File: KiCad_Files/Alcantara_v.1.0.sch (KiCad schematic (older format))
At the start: 21 parts, among them IC3 TLV803EA30DCKR, J5 PJS008U-3000-0, J8 53261-0527, Q1 MMSS8050-H-TP, Q2 MMSS8050-H-TP

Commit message: Add shapes 3D folder
Now all 3D models for the components are stored in a single folder, thanks to the Archive Plugin from https://github.com/MitjaNemec/Kicad_action_plugins.git
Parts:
- C1, C2, C3, C4, C5: symbol Device:C_Small -> archive:Device_C_Small
- IC3: symbol SamacSys_Parts:TLV803EA30DCKR -> archive:SamacSys_Parts_TLV803EA30DCKR
- J5: symbol SamacSys_Parts:PJS008U-3000-0 -> archive:SamacSys_Parts_PJS008U-3000-0
- J8: symbol SamacSys_Parts:53261-0527 -> archive:SamacSys_Parts_53261-0527
- MOD1: symbol dk_RF-Transceiver-Modules:ESP32-WROOM-32 -> archive:dk_RF-Transceiver-Modules_ESP32-WROOM-32
- Q1, Q2: symbol dk_Transistors-Bipolar-BJT-Single:MMSS8050-H-TP -> archive:dk_Transistors-Bipolar-BJT-Single_MMSS8050-H-TP
- R1, R13, R2, R26, R3, R4, R5, R6: symbol Device:R_Small -> archive:Device_R_Small
- S4, S5: symbol SamacSys_Parts:EVP-AAM02W -> archive:SamacSys_Parts_EVP-AAM02W
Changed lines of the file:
@@
 $EndSheet
 $Comp
-L power:GND #PWR01
+L archive:power_GND #PWR01
 U 1 1 61138544
 P 2350 3750
@@
 	2400 3700 2500 3700
 $Comp
-L Device:C_Small C5
+L archive:Device_C_Small C5
 U 1 1 61143841
 P 7900 1575
@@
 $EndComp
 $Comp
-L power:GND #PWR06
+L archive:power_GND #PWR06
 U 1 1 61144448
 P 7900 1875
@@
 	7900 1475 7900 1275
 $Comp
-L power:+3V3 #PWR07
+L archive:power_+3V3 #PWR07
 U 1 1 61144E10
 P 7900 975
@@
 $EndComp
 $Comp
-L Device:R_Small R4
+L archive:Device_R_Small R4
 U 1 1 6114538C
 P 7900 1125
@@
 	9750 5650 9850 5650
 $Comp
-L dk_RF-Transceiver-Modules:ESP32-WROOM-32 MOD1
+L archive:dk_RF-Transceiver-Modules_ESP32-WROOM-32 MOD1
 U 1 1 60CDB9CF
 P 2200 1500
@@
 	3150 1000 3150 1050
 $Comp
-L power:GND #PWR04
+L archive:power_GND #PWR04
 U 1 1 6114294E
 P 3150 1250
@@
 $EndComp
 $Comp
-L Device:C_Small C2
+L archive:Device_C_Small C2
 U 1 1 61142948
 P 3150 1150
@@
 	2700 1000 2700 1050
 $Comp
-L power:GND #PWR02
+L archive:power_GND #PWR02
 U 1 1 611407CF
 P 2700 1250
@@
 $EndComp
 $Comp
-L Device:C_Small C1
+L archive:Device_C_Small C1
 U 1 1 611407C9
 P 2700 1150
@@
 $EndComp
 $Comp
-L power:+3V3 #PWR03
+L archive:power_+3V3 #PWR03
 U 1 1 61138053
 P 3150 950
@@
 	2400 1000 2700 1000
 $Comp
-L Device:C_Small C4
+L archive:Device_C_Small C4
 U 1 1 611FBCA3
 P 7550 1575
@@
 	9750 5000 9850 5000
 $Comp
-L dk_Transistors-Bipolar-BJT-Single:MMSS8050-H-TP Q1
+L archive:dk_Transistors-Bipolar-BJT-Single_MMSS8050-H-TP Q1
 U 1 1 61214E60
 P 5800 4875
@@
 $EndComp
 $Comp
-L dk_Transistors-Bipolar-BJT-Single:MMSS8050-H-TP Q2
+L archive:dk_Transistors-Bipolar-BJT-Single_MMSS8050-H-TP Q2
 U 1 1 61215ACB
 P 5800 5475
@@
 $EndComp
 $Comp
-L Device:R_Small R1
+L archive:Device_R_Small R1
 U 1 1 61216528
 P 5450 4875
@@
 $EndComp
 $Comp
-L Device:R_Small R2
+L archive:Device_R_Small R2
 U 1 1 61216A1C
 P 5450 5475
@@
 	7900 1275 8100 1275
 $Comp
-L power:GND #PWR05
+L archive:power_GND #PWR05
 U 1 1 612BFDFC
 P 5900 3650
@@
 $EndComp
 $Comp
-L Device:C_Small C3
+L archive:Device_C_Small C3
 U 1 1 612BFE20
 P 5900 3300
@@
 	3100 3000 3150 3000
 $Comp
-L power:+3V3 #PWR053
+L archive:power_+3V3 #PWR053
 U 1 1 614C013F
 P 7075 3425
@@
 $EndComp
 $Comp
-L power:+5V #PWR051
+L archive:power_+5V #PWR051
 U 1 1 614C4F85
 P 8375 3425
@@
 	7525 3525 7525 3375
 $Comp
-L power:GND #PWR052
+L archive:power_GND #PWR052
 U 1 1 614FBA5A
 P 7725 3675
@@
 	3650 2500 3650 2400
 $Comp
-L SamacSys_Parts:EVP-AAM02W S5
+L archive:SamacSys_Parts_EVP-AAM02W S5
 U 1 1 60E2AB97
 P 4450 3250
@@
 	5700 3350 5700 3550
 $Comp
-L SamacSys_Parts:EVP-AAM02W S4
+L archive:SamacSys_Parts_EVP-AAM02W S4
 U 1 1 60E6112B
 P 6100 1525
@@
 NoConn ~ 4750 7025
 $Comp
-L power:GND #PWR0103
+L archive:power_GND #PWR0103
 U 1 1 6126E144
 P 4850 7425
@@
 $EndComp
 $Comp
-L power:+3V3 #PWR0104
+L archive:power_+3V3 #PWR0104
 U 1 1 6126EAE6
 P 3550 6475
@@
 	3550 7025 3650 7025
 $Comp
-L Device:R_Small R3
+L archive:Device_R_Small R3
 U 1 1 612A0089
 P 3450 6725
@@
 	3650 5350 3850 5350
 $Comp
-L Device:R_Small R6
+L archive:Device_R_Small R6
 U 1 1 61313692
 P 3850 5150
@@
 	3850 5350 3850 5250
 $Comp
-L power:+3V3 #PWR0105
+L archive:power_+3V3 #PWR0105
 U 1 1 6134BA7C
 P 3850 4950
@@
 GPS_ON_OFF
 $Comp
-L Device:R_Small R5
+L archive:Device_R_Small R5
 U 1 1 6158FB54
 P 5250 6975
@@
 $EndComp
 $Comp
-L SamacSys_Parts:PJS008U-3000-0 J5
+L archive:SamacSys_Parts_PJS008U-3000-0 J5
 U 1 1 612F4333
 P 4200 7125
@@
 $EndComp
 $Comp
-L SamacSys_Parts:53261-0527 J8
+L archive:SamacSys_Parts_53261-0527 J8
 U 1 1 61489378
 P 7525 2525
@@
 	4750 7225 5250 7225
 $Comp
-L Device:R_Small R26
+L archive:Device_R_Small R26
 U 1 1 61524AEC
 P 4900 6975
@@
 $EndComp
 $Comp
-L Device:R_Small R13
+L archive:Device_R_Small R13
 U 1 1 61547DCC
 P 3150 6725
@@
 Connection ~ 3450 6525
 $Comp
-L power:+3V3 #PWR0107
+L archive:power_+3V3 #PWR0107
 U 1 1 615572C8
 P 4900 6775
@@
 	7075 3425 7075 3525
 $Comp
-L SamacSys_Parts:TLV803EA30DCKR IC3
+L archive:SamacSys_Parts_TLV803EA30DCKR IC3
 U 1 1 612F7BFE
 P 6300 1325
@@
 	7350 1825 7550 1825
 $Comp
-L power:GND #PWR0116
+L archive:power_GND #PWR0116
 U 1 1 615212CE
 P 5550 1775
@@
 Connection ~ 6250 1275
 $Comp
-L power:+3V3 #PWR0117
+L archive:power_+3V3 #PWR0117
 U 1 1 6153412D
 P 5050 1225

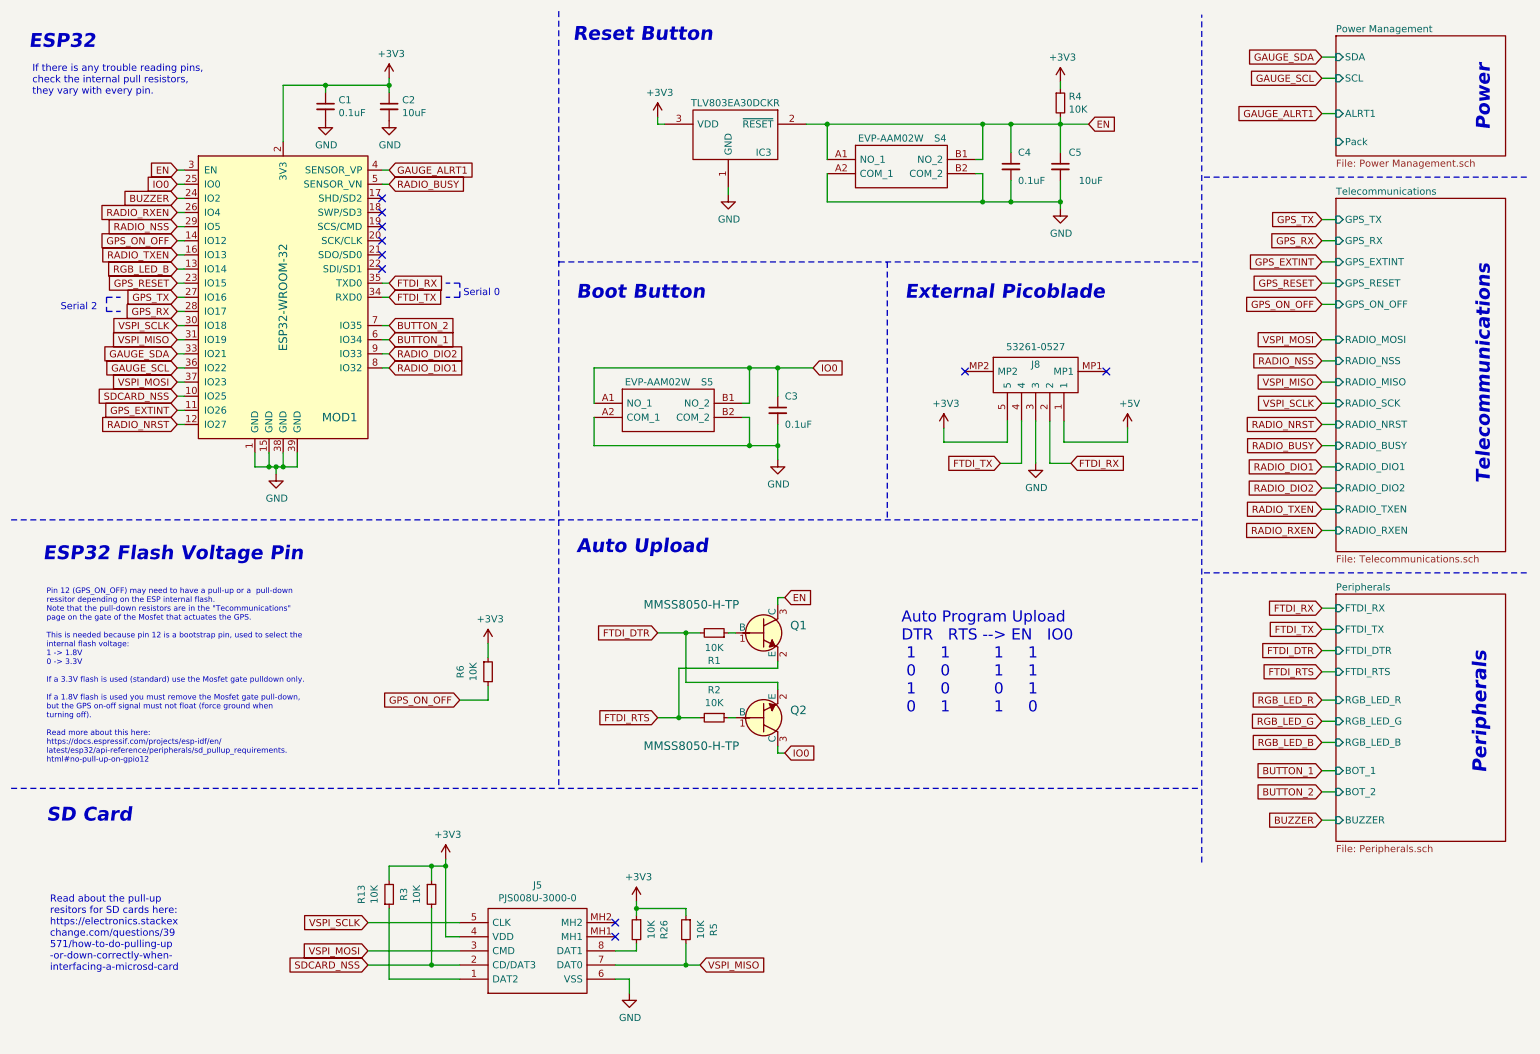
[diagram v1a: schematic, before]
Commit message: Realocated and replaced components
Components where replaced because of the chip shortage, such as the 3.3 V Voltage regulator, the USB ESD protector and the SD Card holder.

The ESP32 has been rotated and moved closer to the center of the board, now having it's antenna positioned outside of the original board outline, providing better range for the Bluetooth and Wi-Fi.
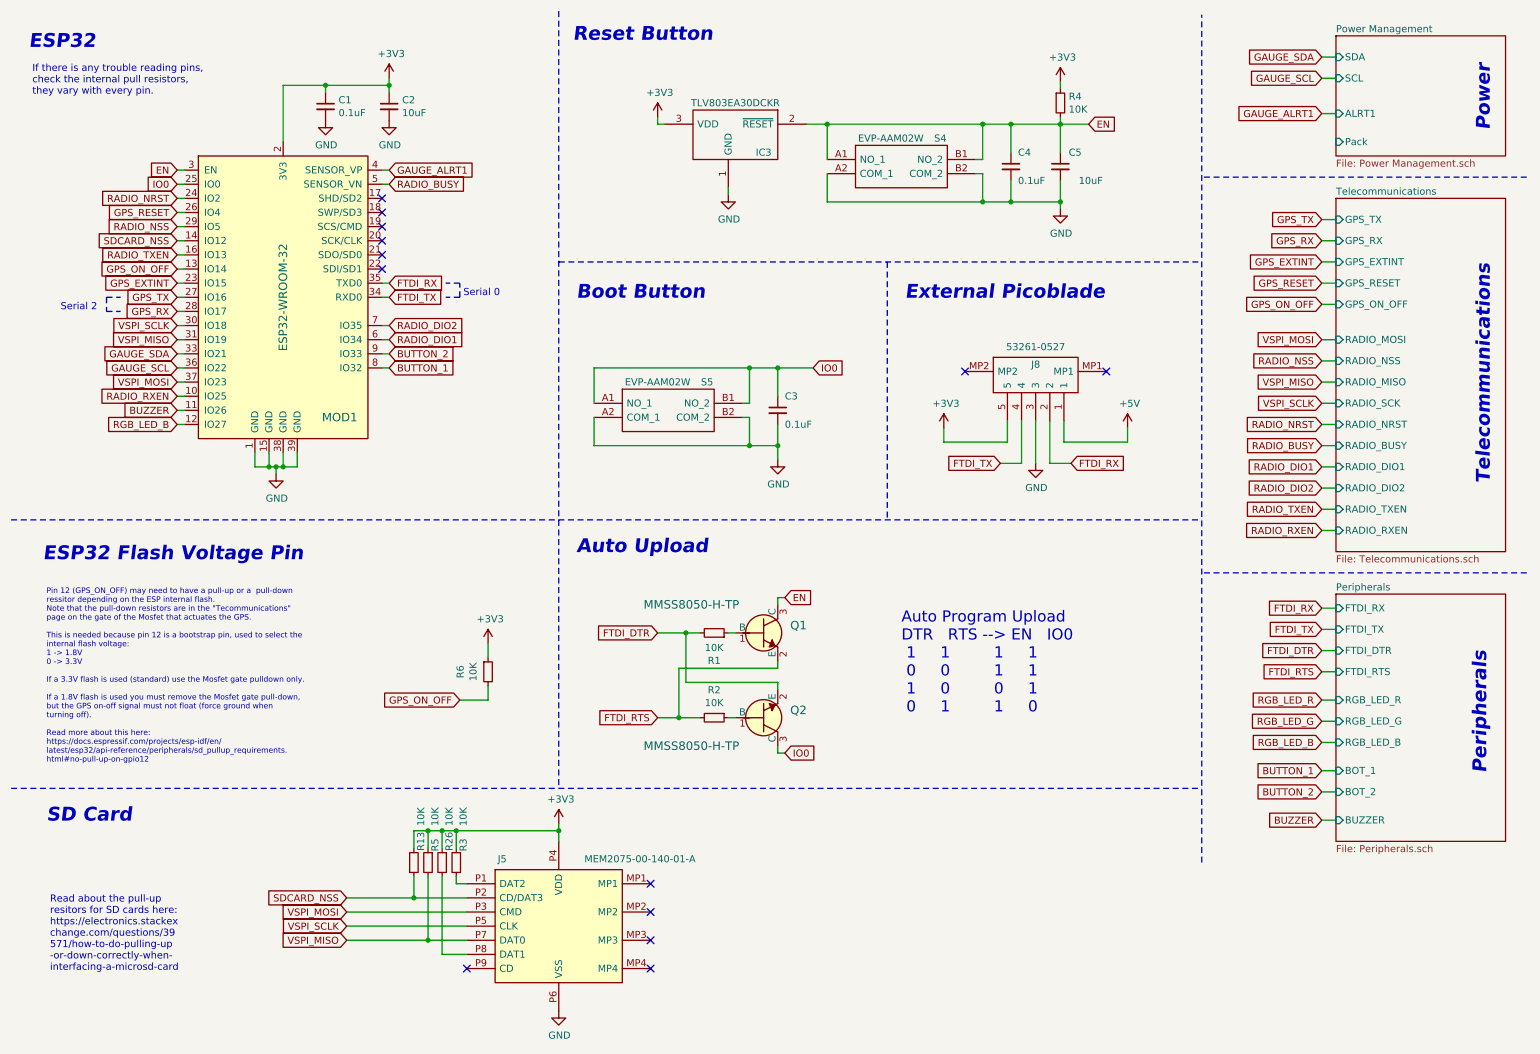
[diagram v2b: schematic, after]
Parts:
- removed J5: PJS008U-3000-0, SamacSys_Parts:PJS008U30000, symbol archive:SamacSys_Parts_PJS008U-3000-0
- added J5: MEM2075-00-140-01-A, SamacSys_Parts:MEM20750014001A, symbol SamacSys_Parts:MEM2075-00-140-01-A
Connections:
- net +3V3: now also J5.P4 (VDD)
- net BUTTON_1: now also MOD1.8 (IO32); no longer MOD1.6 (IO34)
- net BUTTON_2: now also MOD1.9 (IO33); no longer MOD1.7 (IO35)
- net BUZZER: now also MOD1.11 (IO26); no longer MOD1.24 (IO2)
- net GND: now also J5.P6 (VSS)
- net GPS_EXTINT: now also MOD1.23 (IO15); no longer MOD1.11 (IO26)
- net GPS_ON_OFF: now also MOD1.13 (IO14); no longer MOD1.14 (IO12)
- net GPS_RESET: now also MOD1.26 (IO4); no longer MOD1.23 (IO15)
- net RADIO_DIO1: now also MOD1.6 (IO34); no longer MOD1.8 (IO32)
- net RADIO_DIO2: now also MOD1.7 (IO35); no longer MOD1.9 (IO33)
- net RADIO_NRST: now also MOD1.24 (IO2); no longer MOD1.12 (IO27)
- net RADIO_RXEN: now also MOD1.10 (IO25); no longer MOD1.26 (IO4)
- net RGB_LED_B: now also MOD1.12 (IO27); no longer MOD1.13 (IO14)
- net SDCARD_NSS: now also MOD1.14 (IO12), R13.1, J5.P2 (CD/DAT3); no longer MOD1.10 (IO25), R3.2
- net VSPI_MISO: now also J5.P7 (DAT0)
- net VSPI_MOSI: now also J5.P3 (CMD)
- net VSPI_SCLK: now also J5.P5 (CLK)
- net at R26.2: now also J5.P8 (DAT1)
- new net: J5.P1 (DAT2), R3.2
- no-connect marks 10 -> 13
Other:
- moved on the sheet: R13, R26, R3, R5

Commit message: Reduces board length to 101,5 mm
JLC PCB allows a 4 layer PCB to be manufactured for just $8,00 if it is within 102 x 102 mm. The previous version was 105,47 mm, making it cost $37,00.

To reduce the manufacturing cost the board had its size cut down to 101,5 mm. This was possible by moving the buzzer from the top left corner of the board to the free space between the two SMA connectors.
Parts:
- J5: symbol SamacSys_Parts:MEM2075-00-140-01-A -> archive:SamacSys_Parts_MEM2075-00-140-01-A
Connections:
- net BUZZER: now also MOD1.16 (IO13); no longer MOD1.11 (IO26)
- net GPS_ON_OFF: now also MOD1.12 (IO27); no longer MOD1.13 (IO14)
- net RADIO_TXEN: now also MOD1.11 (IO26); no longer MOD1.16 (IO13)
- net RGB_LED_B: now also MOD1.14 (IO12); no longer MOD1.12 (IO27)
- net SDCARD_NSS: now also MOD1.13 (IO14); no longer MOD1.14 (IO12)
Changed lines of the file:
@@
 NoConn ~ 3100 1900
 NoConn ~ 3100 1800
-Text GLabel 1650 3400 0    50   Input ~ 0
+Text GLabel 1650 2100 0    50   Input ~ 0
 RGB_LED_B
 Text GLabel 3150 3000 2    50   Input ~ 0
@@
 Text GLabel 3150 2700 2    50   Input ~ 0
 RADIO_DIO2
-Text GLabel 1650 2200 0    50   Input ~ 0
+Text GLabel 1650 3300 0    50   Input ~ 0
 RADIO_TXEN
 Text GLabel 1650 3200 0    50   Input ~ 0
@@
 Wire Wire Line
 	1650 3400 1700 3400
-Text GLabel 1650 3300 0    50   Input ~ 0
+Text GLabel 1650 2200 0    50   Input ~ 0
 BUZZER
 Wire Wire Line
@@
 Wire Wire Line
 	7350 1625 7350 1825
+Text GLabel 1650 3400 0    50   Input ~ 0
+GPS_ON_OFF
 Text GLabel 1650 2300 0    50   Input ~ 0
-GPS_ON_OFF
-Text GLabel 1650 2100 0    50   Input ~ 0
 SDCARD_NSS
 Wire Wire Line
@@
 	4350 475  4350 5975
 $Comp
-L SamacSys_Parts:MEM2075-00-140-01-A J5
+L archive:SamacSys_Parts_MEM2075-00-140-01-A J5
 U 1 1 6204CE35
 P 3700 6650
